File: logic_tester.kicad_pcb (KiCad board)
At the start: 2 copper layers, 68 x 12 mm, 37 parts, among them J1 15EDGR-3.5-02P, J2 Probe, U1 LM339D, U2 LM317MDT

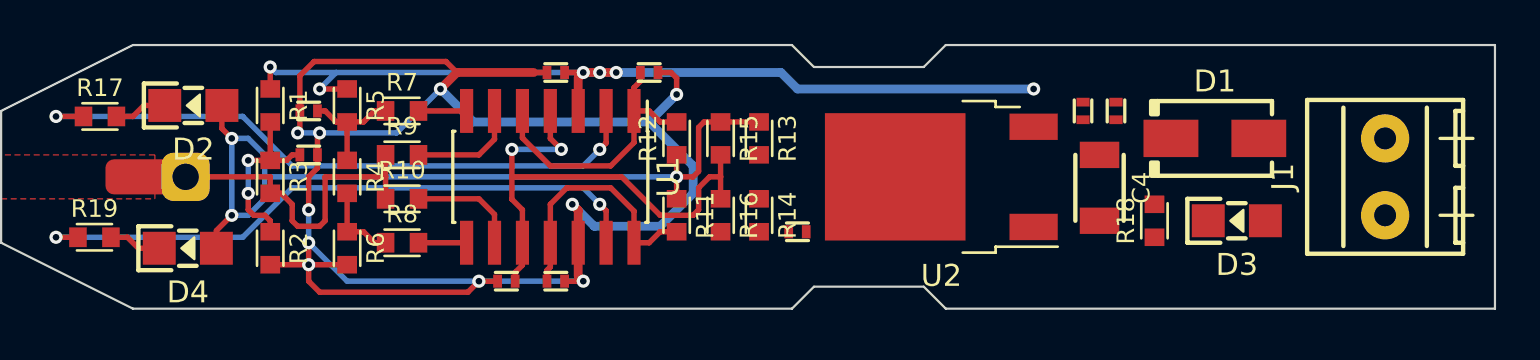
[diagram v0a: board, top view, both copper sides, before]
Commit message: Routing done. PCB shortened
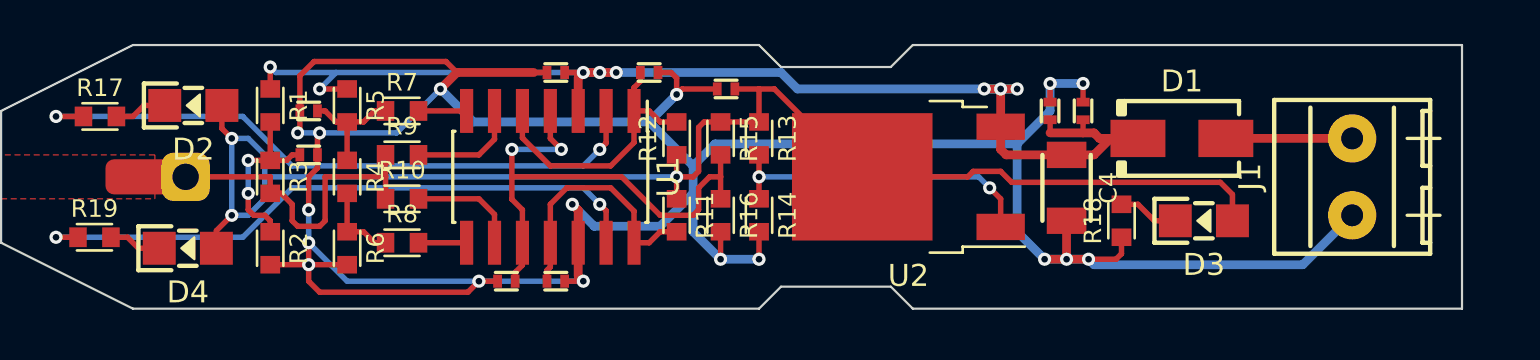
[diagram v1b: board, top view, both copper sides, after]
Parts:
- moved C9 7.27 mm to (108.0, 96.0)
- moved C4 1.50 mm to (123.5, 100.5)
- moved C5 1.50 mm to (124.2, 97.0)
- moved C6 1.50 mm to (122.8, 97.0)
- moved D1 1.50 mm to (128.8, 98.2)
- moved D3 1.50 mm to (129.8, 102.0)
- moved J1 1.50 mm to (136.5, 100.0)
- moved R18 1.50 mm to (126.0, 102.0)
- moved U2 1.50 mm to (116.3, 100.0)
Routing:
- net GNDD: track 84.2 -> 142.6 mm, vias 10 -> 17
- net /VCC_REG: track 39.3 -> 66.9 mm
- net V+: track 42.7 -> 59.6 mm, vias 6 -> 8
- net Net-(U2-ADJ): track 0.00 -> 14.7 mm, vias 0 -> 2
- net Net-(D1-A): track 0.00 -> 5.75 mm
- net Net-(D3-K): track 0.00 -> 2.76 mm
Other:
- board size 68 x 12 mm -> 66.5 x 12 mm

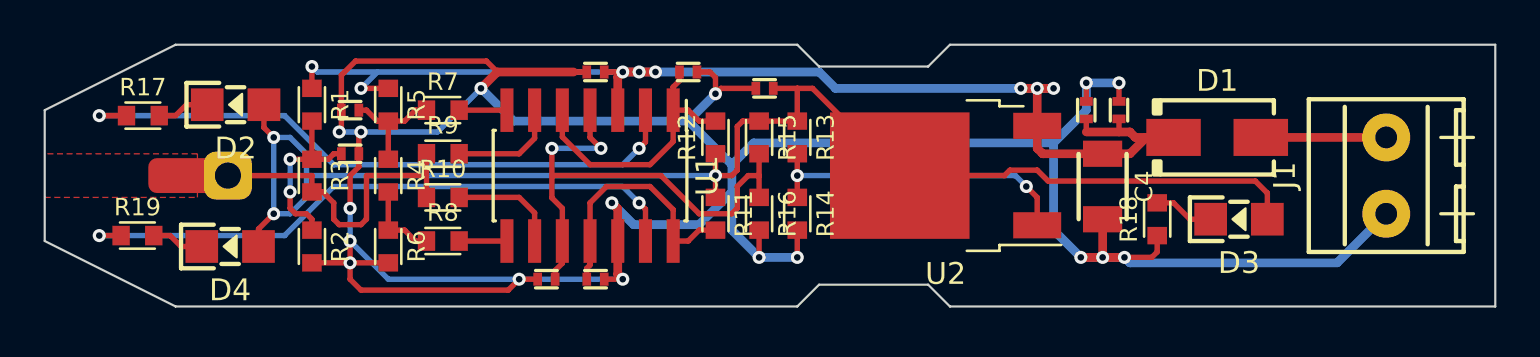
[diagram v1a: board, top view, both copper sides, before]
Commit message: Size changed: 66x12
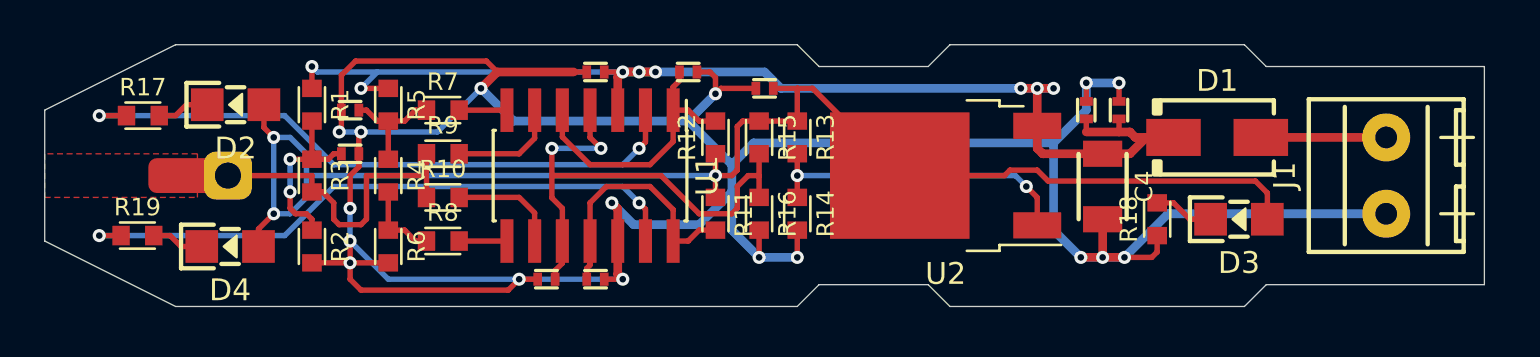
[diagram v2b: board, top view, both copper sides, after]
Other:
- board size 66.5 x 12 mm -> 66 x 12 mm
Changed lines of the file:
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@@
   )
   (gr_line (start 81 106) (end 109.5 106)
-    (stroke (width 0.1) (type default)) (layer "Edge.Cuts"))
+    (stroke (width 0.05) (type default)) (layer "Edge.Cuts"))
   (gr_line (start 75 103) (end 81 106)
-    (stroke (width 0.1) (type default)) (layer "Edge.Cuts"))
+    (stroke (width 0.05) (type default)) (layer "Edge.Cuts"))
   (gr_line (start 109.5 106) (end 110.5 105)
-    (stroke (width 0.1) (type default)) (layer "Edge.Cuts"))
+    (stroke (width 0.05) (type default)) (layer "Edge.Cuts"))
+  (gr_line (start 130 106) (end 131 105)
+    (stroke (width 0.05) (type default)) (layer "Edge.Cuts"))
   (gr_line (start 110.5 95) (end 109.5 94)
-    (stroke (width 0.1) (type default)) (layer "Edge.Cuts"))
+    (stroke (width 0.05) (type default)) (layer "Edge.Cuts"))
   (gr_line (start 75 97) (end 75 103)
-    (stroke (width 0.1) (type default)) (layer "Edge.Cuts"))
+    (stroke (width 0.05) (type default)) (layer "Edge.Cuts"))
   (gr_line (start 110.5 105) (end 115.5 105)
-    (stroke (width 0.1) (type default)) (layer "Edge.Cuts"))
+    (stroke (width 0.05) (type default)) (layer "Edge.Cuts"))
   (gr_line (start 115.5 95) (end 110.5 95)
-    (stroke (width 0.1) (type default)) (layer "Edge.Cuts"))
-  (gr_line (start 141.5 106) (end 141.5 94)
-    (stroke (width 0.1) (type default)) (layer "Edge.Cuts"))
+    (stroke (width 0.05) (type default)) (layer "Edge.Cuts"))
+  (gr_line (start 141 105) (end 141 95)
+    (stroke (width 0.05) (type default)) (layer "Edge.Cuts"))
   (gr_line (start 116.5 94) (end 115.5 95)
-    (stroke (width 0.1) (type default)) (layer "Edge.Cuts"))
-  (gr_line (start 141.5 94) (end 116.5 94)
-    (stroke (width 0.1) (type default)) (layer "Edge.Cuts"))
+    (stroke (width 0.05) (type default)) (layer "Edge.Cuts"))
+  (gr_line (start 130 94) (end 131 95)
+    (stroke (width 0.05) (type default)) (layer "Edge.Cuts"))
+  (gr_line (start 130 94) (end 116.5 94)
+    (stroke (width 0.05) (type default)) (layer "Edge.Cuts"))
+  (gr_line (start 131 95) (end 141 95)
+    (stroke (width 0.05) (type default)) (layer "Edge.Cuts"))
   (gr_line (start 115.5 105) (end 116.5 106)
-    (stroke (width 0.1) (type default)) (layer "Edge.Cuts"))
-  (gr_line (start 116.5 106) (end 141.5 106)
-    (stroke (width 0.1) (type default)) (layer "Edge.Cuts"))
+    (stroke (width 0.05) (type default)) (layer "Edge.Cuts"))
+  (gr_line (start 116.5 106) (end 130 106)
+    (stroke (width 0.05) (type default)) (layer "Edge.Cuts"))
   (gr_line (start 109.5 94) (end 81 94)
-    (stroke (width 0.1) (type default)) (layer "Edge.Cuts"))
+    (stroke (width 0.05) (type default)) (layer "Edge.Cuts"))
+  (gr_line (start 131 105) (end 141 105)
+    (stroke (width 0.05) (type default)) (layer "Edge.Cuts"))
   (gr_line (start 75 97) (end 81 94)
-    (stroke (width 0.1) (type default)) (layer "Edge.Cuts"))
+    (stroke (width 0.05) (type default)) (layer "Edge.Cuts"))
   (segment (start 104.1 95.65) (end 104.1 95.25) (width 0.25) (layer "F.Cu") (net 1))
   (segment (start 98.73 97) (end 98.73 98.23) (width 0.25) (layer "F.Cu") (net 1))
@@
   (segment (start 104.5 97.5) (end 96.5 97.5) (width 0.4) (layer "B.Cu") (net 2))
   (segment (start 106.5 100.75) (end 106.5 99.5) (width 0.4) (layer "B.Cu") (net 2))
-  (segment (start 134.25 104) (end 124.75 104) (width 0.4) (layer "B.Cu") (net 2))
   (segment (start 122.5 103.75) (end 121.25 102.5) (width 0.4) (layer "B.Cu") (net 2))
   (segment (start 88.5 98) (end 89.5 98) (width 0.25) (layer "B.Cu") (net 2))
@@
   (segment (start 106.5 99.5) (end 104.5 97.5) (width 0.4) (layer "B.Cu") (net 2))
   (segment (start 96.5 97.5) (end 95 96) (width 0.4) (layer "B.Cu") (net 2))
+  (segment (start 136.5 101.75) (end 126.5 101.75) (width 0.4) (layer "B.Cu") (net 2))
   (segment (start 96.75 104.75) (end 90.75 104.75) (width 0.25) (layer "B.Cu") (net 2))
   (segment (start 105 102.25) (end 106.5 100.75) (width 0.4) (layer "B.Cu") (net 2))
@@
   (segment (start 101 101.25) (end 102 102.25) (width 0.4) (layer "B.Cu") (net 2))
   (segment (start 109.5 103.75) (end 107.75 103.75) (width 0.4) (layer "B.Cu") (net 2))
+  (segment (start 126.5 101.75) (end 124.5 103.75) (width 0.4) (layer "B.Cu") (net 2))
   (segment (start 102 102.25) (end 105 102.25) (width 0.4) (layer "B.Cu") (net 2))
   (segment (start 124.5 103.75) (end 122.5 103.75) (width 0.4) (layer "B.Cu") (net 2))
-  (segment (start 124.75 104) (end 124.5 103.75) (width 0.4) (layer "B.Cu") (net 2))
   (segment (start 89 101.5) (end 89 103) (width 0.25) (layer "B.Cu") (net 2))
-  (segment (start 136.5 101.75) (end 134.25 104) (width 0.4) (layer "B.Cu") (net 2))
   (segment (start 106.5 102.5) (end 107.75 103.75) (width 0.4) (layer "B.Cu") (net 2))
   (segment (start 106.5 100.75) (end 106.5 102.5) (width 0.4) (layer "B.Cu") (net 2))
@@
   (segment (start 120.5 96) (end 121.25 96) (width 0.4) (layer "B.Cu") (net 7))
   (segment (start 90.25 95.25) (end 87.5 95.25) (width 0.25) (layer "B.Cu") (net 7))
+  (segment (start 108 95.25) (end 103 95.25) (width 0.4) (layer "B.Cu") (net 7))
   (segment (start 87.5 95.25) (end 87.25 95) (width 0.25) (layer "B.Cu") (net 7))
+  (segment (start 108.75 96) (end 108 95.25) (width 0.4) (layer "B.Cu") (net 7))
   (segment (start 90.25 95.25) (end 89.5 96) (width 0.25) (layer "B.Cu") (net 7))
-  (segment (start 111.25 96) (end 121.25 96) (width 0.4) (layer "B.Cu") (net 7))
   (segment (start 120.5 96) (end 119.75 96) (width 0.4) (layer "B.Cu") (net 7))
-  (segment (start 110.5 95.25) (end 111.25 96) (width 0.4) (layer "B.Cu") (net 7))
   (segment (start 101.5 95.25) (end 90.25 95.25) (width 0.25) (layer "B.Cu") (net 7))
-  (segment (start 103 95.25) (end 110.5 95.25) (width 0.4) (layer "B.Cu") (net 7))
+  (segment (start 121.25 96) (end 108.75 96) (width 0.4) (layer "B.Cu") (net 7))
   (segment (start 101.5 95.25) (end 103 95.25) (width 0.4) (layer "B.Cu") (net 7))
   (segment (start 131.05 102) (end 131.05 100.8) (width 0.25) (layer "F.Cu") (net 8))

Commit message: Silk work
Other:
- board text added: "0"
- board text added: "1"
- board text added: "HIGH"
- board text added: "LOW"
- board text added: "POWER"
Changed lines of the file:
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@@
     (property "ki_keywords" "R res resistor")
     (attr smd)
-    (fp_text reference "R10" (at 0 -1.3) (layer "F.SilkS")
+    (fp_text reference "R10" (at 0 -1.3) (layer "F.SilkS") hide
         (effects (font (size 0.8 0.8) (thickness 0.15)))
     )
@@
     (property "ki_keywords" "R res resistor")
     (attr smd)
-    (fp_text reference "R8" (at 0 -1.3) (layer "F.SilkS")
+    (fp_text reference "R8" (at 0 -1.3) (layer "F.SilkS") hide
         (effects (font (size 0.8 0.8) (thickness 0.15)))
     )
@@
     (property "ki_keywords" "screw terminal")
     (attr through_hole)
-    (fp_text reference "J1" (at 0 -4.65 90) (layer "F.SilkS")
+    (fp_text reference "J1" (at 0 -4.65 90) (layer "F.SilkS") hide
         (effects (font (size 1 1) (thickness 0.15)))
     )
@@
     (property "ki_keywords" "R res resistor")
     (attr smd)
-    (fp_text reference "R15" (at 0 -1.3 90) (layer "F.SilkS")
+    (fp_text reference "R15" (at 0 -1.3 90) (layer "F.SilkS") hide
         (effects (font (size 0.8 0.8) (thickness 0.15)))
     )
@@
     (zone_connect 1)
     (attr smd)
-    (fp_text reference "D4" (at 0 2 180) (layer "F.SilkS")
+    (fp_text reference "D4" (at 0 2 180) (layer "F.SilkS") hide
         (effects (font (size 1 1) (thickness 0.15)))
     )
@@
     (property "ki_keywords" "R res resistor")
     (attr smd)
-    (fp_text reference "R13" (at 0 -1.3 90) (layer "F.SilkS")
+    (fp_text reference "R13" (at 0 -1.3 90) (layer "F.SilkS") hide
         (effects (font (size 0.8 0.8) (thickness 0.15)))
     )
@@
     (property "ki_keywords" "R res resistor")
     (attr smd)
-    (fp_text reference "R12" (at 0 -1.3 90) (layer "F.SilkS")
+    (fp_text reference "R12" (at 0 -1.3 90) (layer "F.SilkS") hide
         (effects (font (size 0.8 0.8) (thickness 0.15)))
     )
@@
     (property "ki_keywords" "R res resistor")
     (attr smd)
-    (fp_text reference "R4" (at 0 -1.3 90) (layer "F.SilkS")
+    (fp_text reference "R4" (at 0 -1.3 90) (layer "F.SilkS") hide
         (effects (font (size 0.8 0.8) (thickness 0.15)))
     )
@@
     (property "ki_keywords" "R res resistor")
     (attr smd)
-    (fp_text reference "R3" (at 0 -1.3 90) (layer "F.SilkS")
+    (fp_text reference "R3" (at 0 -1.3 90) (layer "F.SilkS") hide
         (effects (font (size 0.8 0.8) (thickness 0.15)))
     )
@@
     (property "ki_keywords" "R res resistor")
     (attr smd)
-    (fp_text reference "R17" (at 0 -1.3) (layer "F.SilkS")
+    (fp_text reference "R17" (at 0 -1.3) (layer "F.SilkS") hide
         (effects (font (size 0.8 0.8) (thickness 0.15)))
     )
@@
     (property "ki_keywords" "R res resistor")
     (attr smd)
-    (fp_text reference "R16" (at 0 -1.3 90) (layer "F.SilkS")
+    (fp_text reference "R16" (at 0 -1.3 90) (layer "F.SilkS") hide
         (effects (font (size 0.8 0.8) (thickness 0.15)))
     )
@@
     (property "ki_keywords" "R res resistor")
     (attr smd)
-    (fp_text reference "R1" (at 0 -1.3 90) (layer "F.SilkS")
+    (fp_text reference "R1" (at 0 -1.3 90) (layer "F.SilkS") hide
         (effects (font (size 0.8 0.8) (thickness 0.15)))
     )
@@
     (property "ki_keywords" "R res resistor")
     (attr smd)
-    (fp_text reference "R14" (at 0 -1.3 90) (layer "F.SilkS")
+    (fp_text reference "R14" (at 0 -1.3 90) (layer "F.SilkS") hide
         (effects (font (size 0.8 0.8) (thickness 0.15)))
     )
@@
     (zone_connect 1)
     (attr smd)
-    (fp_text reference "D2" (at 0 2 180) (layer "F.SilkS")
+    (fp_text reference "D2" (at 0 2 180) (layer "F.SilkS") hide
         (effects (font (size 1 1) (thickness 0.15)))
     )
@@
     (property "ki_description" "Quad Differential Comparator")
     (attr smd)
-    (fp_text reference "U1" (at 0 -5.365 90) (layer "F.SilkS")
+    (fp_text reference "U1" (at 0 -5.365 90) (layer "F.SilkS") hide
         (effects (font (size 1 1) (thickness 0.15)))
     )
@@
     (property "ki_keywords" "R res resistor")
     (attr smd)
-    (fp_text reference "R7" (at 0 -1.3) (layer "F.SilkS")
+    (fp_text reference "R7" (at 0 -1.3) (layer "F.SilkS") hide
         (effects (font (size 0.8 0.8) (thickness 0.15)))
     )
@@
     (property "ki_keywords" "R res resistor")
     (attr smd)
-    (fp_text reference "R2" (at 0 -1.3 90) (layer "F.SilkS")
+    (fp_text reference "R2" (at 0 -1.3 90) (layer "F.SilkS") hide
         (effects (font (size 0.8 0.8) (thickness 0.15)))
     )
@@
     (property "ki_keywords" "R res resistor")
     (attr smd)
-    (fp_text reference "R5" (at 0 -1.3 90) (layer "F.SilkS")
+    (fp_text reference "R5" (at 0 -1.3 90) (layer "F.SilkS") hide
         (effects (font (size 0.8 0.8) (thickness 0.15)))
     )
@@
     (property "ki_keywords" "R res resistor")
     (attr smd)
-    (fp_text reference "R18" (at 0 -1.3 90) (layer "F.SilkS")
+    (fp_text reference "R18" (at 0 -1.3 90) (layer "F.SilkS") hide
         (effects (font (size 0.8 0.8) (thickness 0.15)))
     )
@@
     (property "ki_keywords" "R res resistor")
     (attr smd)
-    (fp_text reference "R19" (at 0 -1.3) (layer "F.SilkS")
+    (fp_text reference "R19" (at 0 -1.3) (layer "F.SilkS") hide
         (effects (font (size 0.8 0.8) (thickness 0.15)))
     )
@@
     (property "ki_keywords" "R res resistor")
     (attr smd)
-    (fp_text reference "R9" (at 0 -1.3) (layer "F.SilkS")
+    (fp_text reference "R9" (at 0 -1.3) (layer "F.SilkS") hide
         (effects (font (size 0.8 0.8) (thickness 0.15)))
     )
@@
     (property "ki_keywords" "R res resistor")
     (attr smd)
-    (fp_text reference "R6" (at 0 -1.3 90) (layer "F.SilkS")
+    (fp_text reference "R6" (at 0 -1.3 90) (layer "F.SilkS") hide
         (effects (font (size 0.8 0.8) (thickness 0.15)))
     )
@@
     (property "ki_description" "Adjustable Linear Regulator")
     (attr smd)
-    (fp_text reference "U2" (at 0 -4.5) (layer "F.SilkS")
+    (fp_text reference "U2" (at 0 -4.5) (layer "F.SilkS") hide
         (effects (font (size 1 1) (thickness 0.15)))
     )
@@
     (zone_connect 1)
     (attr smd)
-    (fp_text reference "D3" (at 0 2 180) (layer "F.SilkS")
+    (fp_text reference "D3" (at 0 2 180) (layer "F.SilkS") hide
         (effects (font (size 1 1) (thickness 0.15)))
     )
@@
     (property "ki_keywords" "R res resistor")
     (attr smd)
-    (fp_text reference "R11" (at 0 -1.3 90) (layer "F.SilkS")
+    (fp_text reference "R11" (at 0 -1.3 90) (layer "F.SilkS") hide
         (effects (font (size 0.8 0.8) (thickness 0.15)))
     )
@@
     (property "ki_keywords" "diode Schottky")
     (attr smd)
-    (fp_text reference "D1" (at 0 -2.6) (layer "F.SilkS")
+    (fp_text reference "D1" (at 0 -2.6) (layer "F.SilkS") hide
         (effects (font (size 1 1) (thickness 0.15)))
     )
@@
     (property "ki_keywords" "cap capacitor")
     (attr smd)
-    (fp_text reference "C4" (at 0 -1.9 90) (layer "F.SilkS")
+    (fp_text reference "C4" (at 0 -1.9 90) (layer "F.SilkS") hide
         (effects (font (size 0.8 0.8) (thickness 0.15)))
     )
@@
   (gr_line (start 75 97) (end 81 94)
     (stroke (width 0.05) (type default)) (layer "Edge.Cuts"))
+  (gr_text "0\n" (at 76.5 102.25) (layer "F.SilkS")
+    (effects (font (size 1.2 1.2) (thickness 0.2) bold))
+  )
+  (gr_text "HIGH" (at 83.75 94.75) (layer "F.SilkS")
+    (effects (font (size 0.9 0.9) (thickness 0.2) bold))
+  )
+  (gr_text "POWER" (at 129.75 104.25) (layer "F.SilkS")
+    (effects (font (size 0.9 0.9) (thickness 0.2) bold))
+  )
+  (gr_text "1" (at 76.5 97.75) (layer "F.SilkS")
+    (effects (font (size 1.2 1.2) (thickness 0.2) bold))
+  )
+  (gr_text "LOW" (at 83.5 105.25) (layer "F.SilkS")
+    (effects (font (size 0.9 0.9) (thickness 0.2) bold))
+  )
   (segment (start 104.1 95.65) (end 104.1 95.25) (width 0.25) (layer "F.Cu") (net 1))
   (segment (start 98.73 97) (end 98.73 98.23) (width 0.25) (layer "F.Cu") (net 1))
